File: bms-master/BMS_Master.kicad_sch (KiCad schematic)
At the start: 79 parts, among them J1 Conn_PWR, J2 PROG, J3 Conn_Fault, J4 BMS_M_IN, J5 Conn_CAN, J6 Conn_CSR, J7 Conn_CSROUT, J8 Micro_SD_Card, SW1 SW_SPST, U1 AP2204K-ADJ, U2 AP2204K-ADJ, U3 STM32F103C8Tx, U4 BQ79600-Q1, U5 SN65HVD256D, U6 TLV2371DBV, U7 TLV2371DBV, Y1 8M, Y2 32.768k

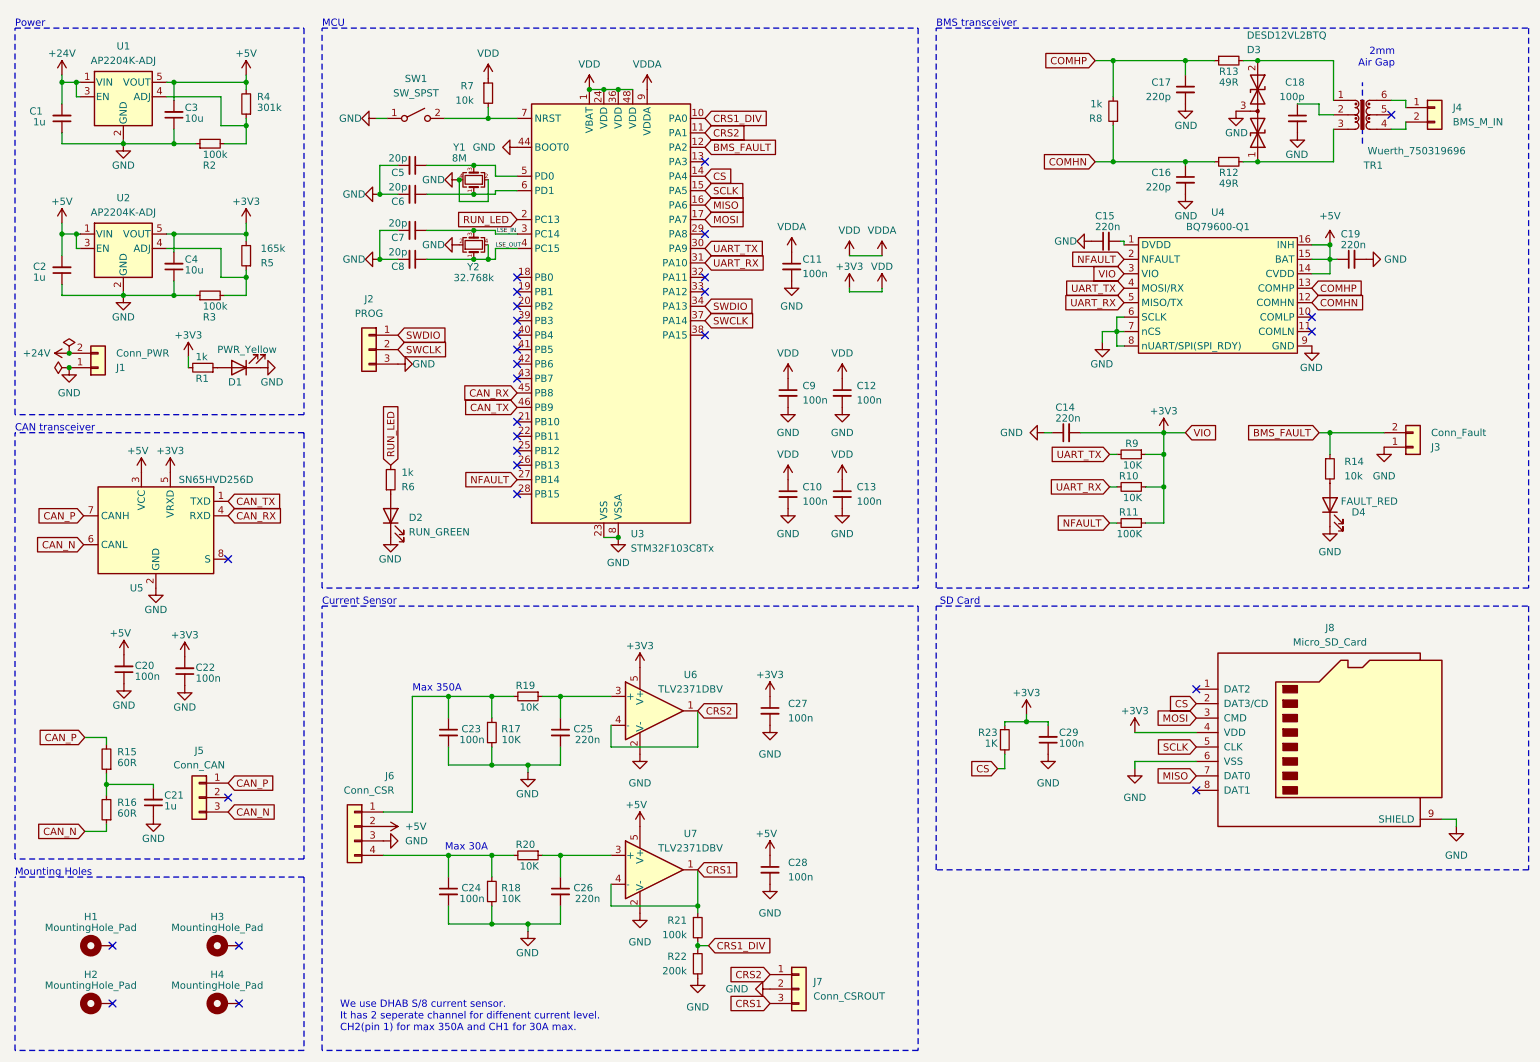
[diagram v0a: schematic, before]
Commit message: feat: wireless BMS and USB power
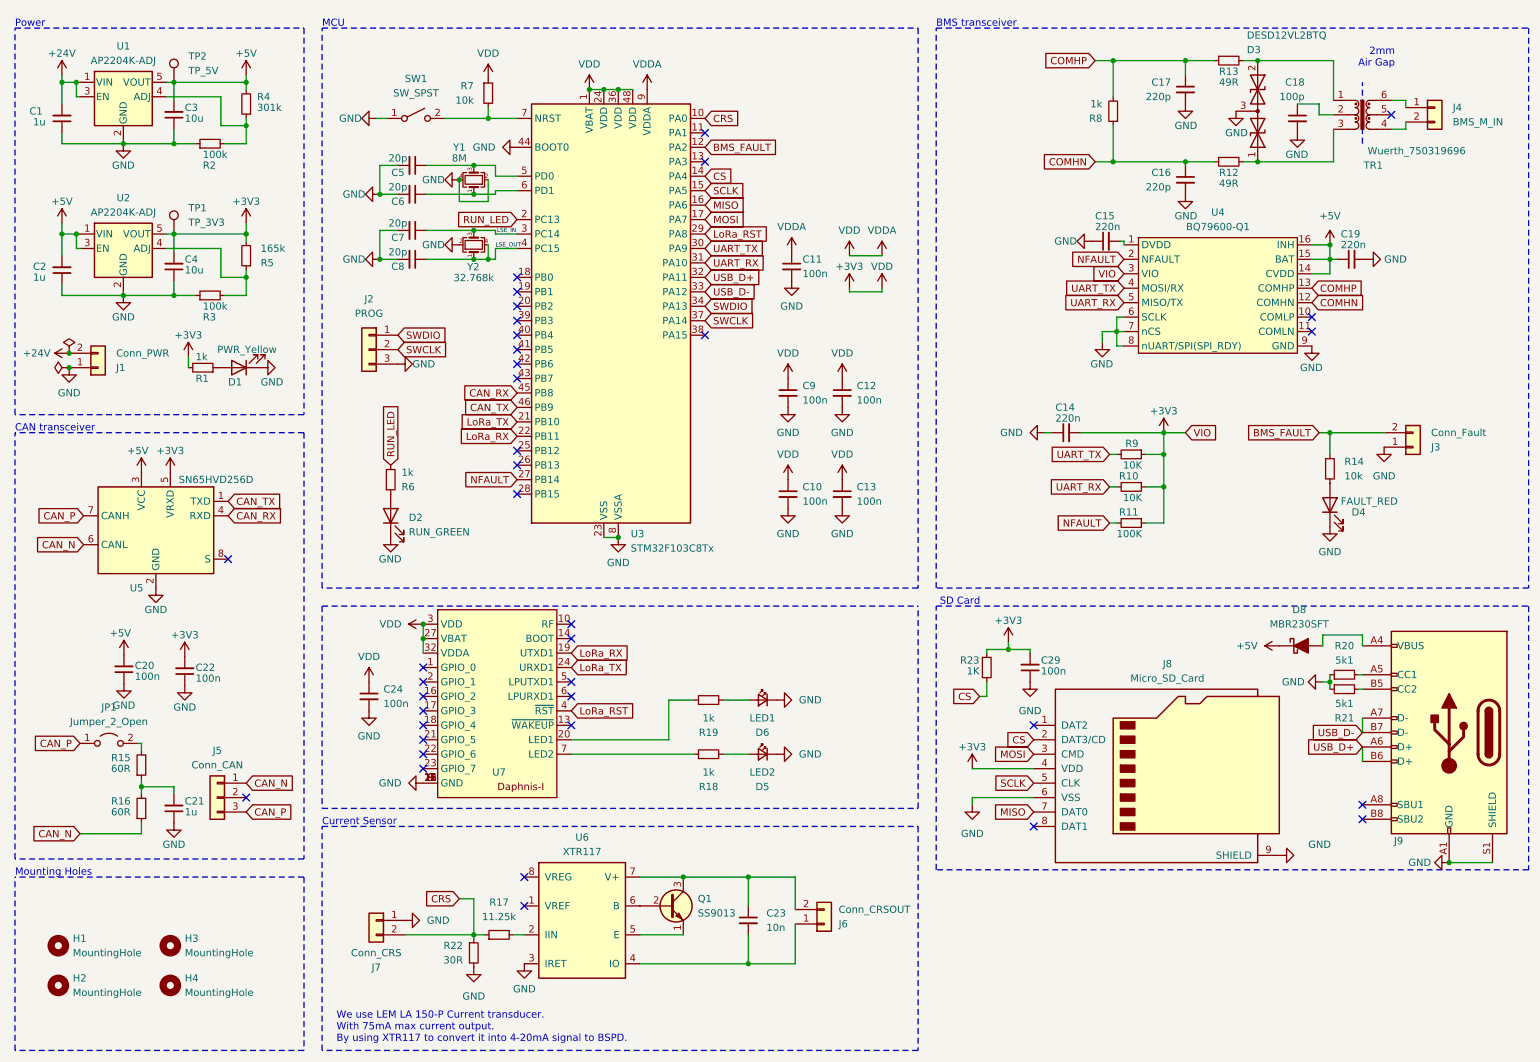
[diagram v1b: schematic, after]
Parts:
- removed C25, C26: 220n, Capacitor_SMD:C_0805_2012Metric, symbol Device:C_Small
- removed C27, C28: 100n, Capacitor_SMD:C_0603_1608Metric, symbol Device:C_Small
- removed H1, H2, H3, H4: MountingHole_Pad, MountingHole:MountingHole_3.2mm_M3_ISO14580_Pad, symbol Mechanical:MountingHole_Pad
- removed J6: Conn_CSR, Connector_JST:JST_XH_B4B-XH-A_1x04_P2.50mm_Vertical, symbol Connector_Generic:Conn_01x04
- removed J7: Conn_CSROUT, Connector_JST:JST_XH_B3B-XH-A_1x03_P2.50mm_Vertical, symbol Connector_Generic:Conn_01x03
- removed U6, U7: TLV2371DBV, Package_TO_SOT_SMD:SOT-23-5, symbol Amplifier_Operational:TLV2371DBV
- added D5: LED2, LED_SMD:LED_0805_2012Metric, symbol Device:LED_Small
- added D6: LED1, LED_SMD:LED_0805_2012Metric, symbol Device:LED_Small
- added D8: MBR230SFT, Diode_SMD:D_SOD-123F, symbol PCM_Diode_Schottky_AKL:MBR230SFT
- added H1, H2, H3, H4: MountingHole, MountingHole:MountingHole_3.2mm_M3_DIN965, symbol Mechanical:MountingHole
- added J6: Conn_CRSOUT, Connector_JST:JST_XH_B2B-XH-A_1x02_P2.50mm_Vertical, symbol Connector_Generic:Conn_01x02
- added J7: Conn_CRS, Connector_JST:JST_XH_B2B-XH-A_1x02_P2.50mm_Vertical, symbol Connector_Generic:Conn_01x02
- added J9: USB_C_Receptacle_USB2.0_16P, Connector_USB:USB_C_Receptacle_Palconn_UTC16-G, symbol Connector:USB_C_Receptacle_USB2.0_16P
- added JP1: Jumper_2_Open, PCM_Jumper_AKL:Jumper_P2.54mm_D0.7mm, symbol Jumper:Jumper_2_Open
- added Q1: SS9013, Package_TO_SOT_SMD:SOT-23, symbol PCM_Transistor_BJT_AKL:SS9013
- added TP1: TP_3V3, Connector_Pin:Pin_D1.0mm_L10.0mm, symbol Connector:TestPoint
- added TP2: TP_5V, Connector_Pin:Pin_D1.0mm_L10.0mm, symbol Connector:TestPoint
- added U6: XTR117, Package_SO:SOIC-8_3.9x4.9mm_P1.27mm, symbol Interface_CurrentLoop:XTR116U
- added U7: ~, Daphnis-I:Daphnis-I, symbol Project_Lib:Daphnis-I
- C23: value 100n -> 10n
- R17: value 10K -> 11.25k
- R18, R19: value 10K -> 1k
- R20: value 10K -> 5k1; footprint Resistor_SMD:R_0603_1608Metric -> Resistor_SMD:R_0603_1608Metric_Pad0.98x0.95mm_HandSolder
- R21: value 100k -> 5k1; footprint Resistor_SMD:R_0603_1608Metric -> Resistor_SMD:R_0603_1608Metric_Pad0.98x0.95mm_HandSolder
- R22: value 200k -> 30R
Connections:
- net CRS1 is gone; now on net GND: R21.1
- net +3V3: now also C24.1, TP1.1, U7.27 (VBAT), U7.3 (VDD), U7.32 (VDDA)
- net +5V: now also D8.1 (K), TP2.1
- net CAN_N: now also J5.1 (Pin_1); no longer J5.3 (Pin_3)
- net CAN_P: now also J5.3 (Pin_3), JP1.1 (A); no longer J5.1 (Pin_1), R15.2
- net GND: now also R20.1, D5.1 (K), D6.1 (K), J7.1 (Pin_1), J9.A1 (GND), J9.A12 (GND), J9.B1 (GND), J9.B12 (GND), J9.S1 (SHIELD), U6.3 (IRET), U7.11 (GND), U7.12 (GND), U7.15 (GND), U7.26 (GND), U7.8 (GND), U7.9 (GND); no longer C23.2, R17.2, R18.2
- net at R19.1: now also U7.20 (LED1)
- net LoRa_TX: now reaches U3.21 (PB10)
- net LoRa_TX: now also U7.24 (URXD1)
- net LoRa_RX: now reaches U3.22 (PB11)
- net LoRa_RX: now also U7.19 (UTXD1)
- net LoRa_RST: now reaches U3.29 (PA8)
- net LoRa_RST: now also U7.4 (~{RST})
- net USB_D+: now reaches U3.32 (PA11)
- net USB_D+: now also J9.A6 (D+), J9.B6 (D+)
- net USB_D-: now reaches U3.33 (PA12)
- net USB_D-: now also J9.A7 (D-), J9.B7 (D-)
- net CRS1_DIV renamed CRS
- net CRS: now also R17.1, J7.2 (Pin_2); no longer R21.2
- net CRS2: no longer names the net of U3.11 (PA1)
- new net: D8.2 (A), J9.A4 (VBUS), J9.A9 (VBUS), J9.B4 (VBUS), J9.B9 (VBUS)
- new net: J9.A5 (CC1), R20.2
- new net: J9.B5 (CC2), R21.2
- new net: JP1.2 (B), R15.2
- new net: R18.1, U7.7 (LED2)
- new net: R17.2, U6.2 (IIN)
- new net: C23.1, J6.2 (Pin_2), Q1.3 (C), U6.7 (V+)
- new net: C23.2, J6.1 (Pin_1), U6.4 (IO)
- new net: D5.2 (A), R18.2
- new net: D6.2 (A), R19.2
- new net: Q1.1 (E), U6.5 (E)
- new net: Q1.2 (B), U6.6 (B)
- no-connect marks 29 -> 38
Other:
- note added: "We use LEM LA 150-P Current transducer. With 75mA max current output. By using XTR117 to convert it into 4-20mA signal to BSPD."
- note removed: "Max 30A"
- note removed: "Max 350A"
- note removed: "We use DHAB S/8 current sensor. It has 2 seperate channel for diffenent current level. CH2(pin 1) for max 350A and CH1 for 30A max."
- moved on the sheet: C21, C29, J5, J8, R15, R16, R22, R23

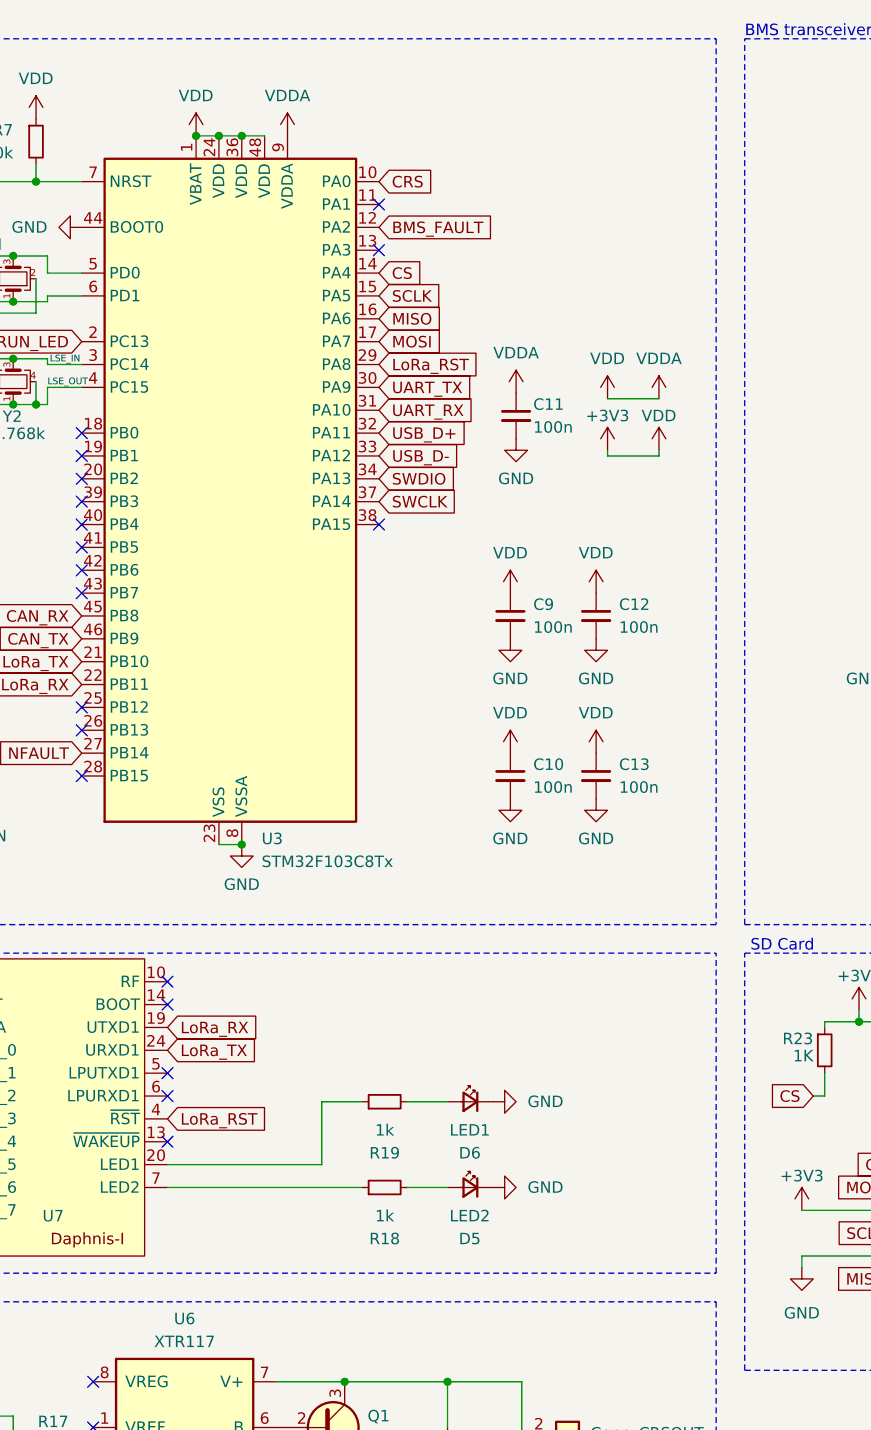
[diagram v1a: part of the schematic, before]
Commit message: fix: USB and USART traces
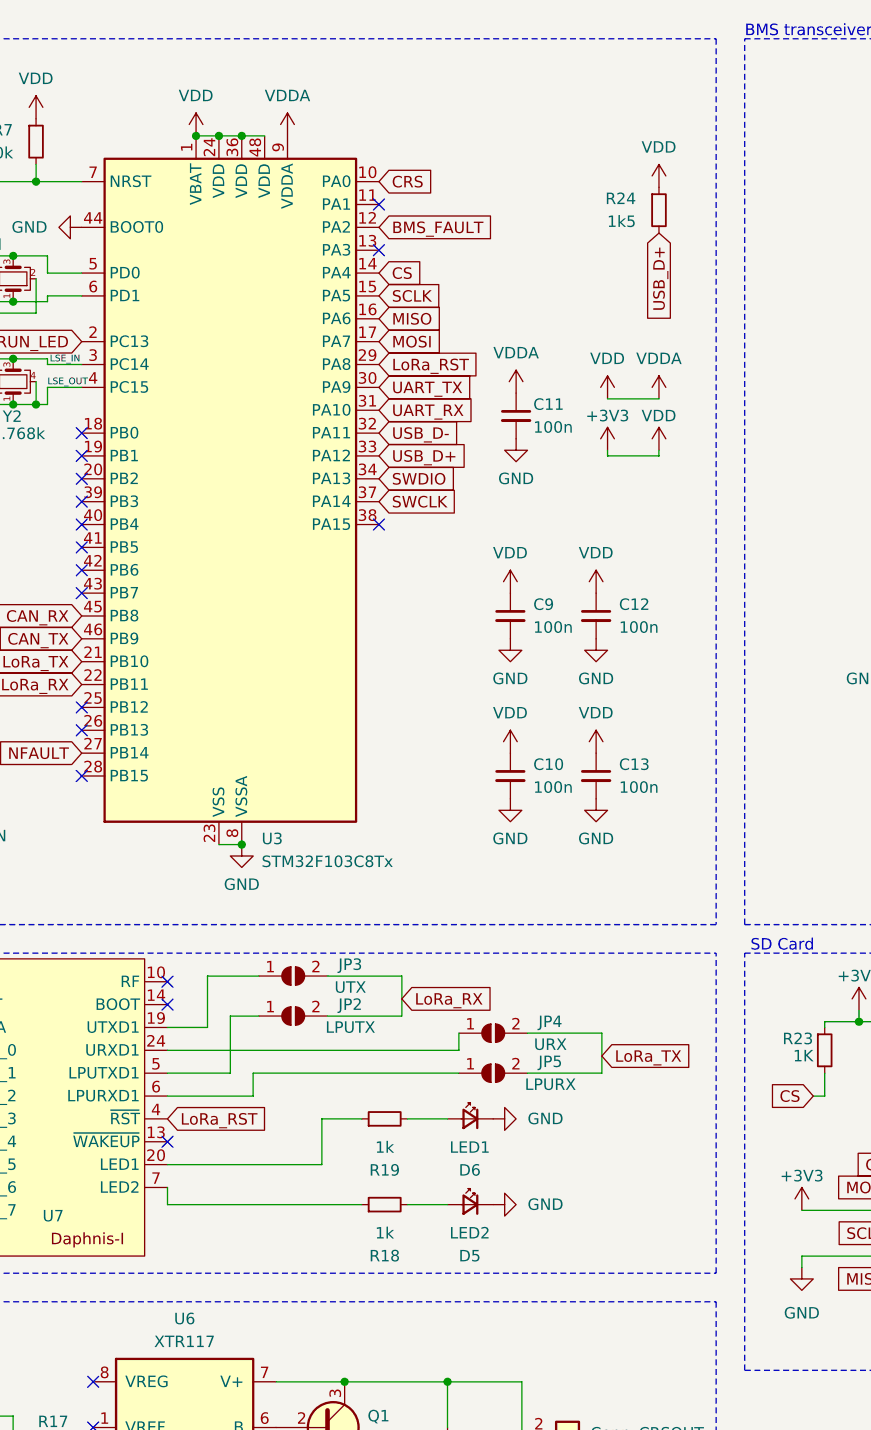
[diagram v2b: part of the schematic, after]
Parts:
- added JP2: LPUTX, Jumper:SolderJumper-2_P1.3mm_Open_RoundedPad1.0x1.5mm, symbol Jumper:SolderJumper_2_Open
- added JP3: UTX, Jumper:SolderJumper-2_P1.3mm_Open_RoundedPad1.0x1.5mm, symbol Jumper:SolderJumper_2_Open
- added JP4: URX, Jumper:SolderJumper-2_P1.3mm_Open_RoundedPad1.0x1.5mm, symbol Jumper:SolderJumper_2_Open
- added JP5: LPURX, Jumper:SolderJumper-2_P1.3mm_Open_RoundedPad1.0x1.5mm, symbol Jumper:SolderJumper_2_Open
- added R24: 1k5, Resistor_SMD:R_0603_1608Metric, symbol Device:R_Small
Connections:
- net +3V3: now also R24.1
- net LoRa_RX: now also JP2.2 (B), JP3.2 (B); no longer U7.19 (UTXD1)
- net LoRa_TX: now also JP4.2 (B), JP5.2 (B); no longer U7.24 (URXD1)
- net USB_D+: now also U3.33 (PA12), R24.2; no longer U3.32 (PA11)
- net USB_D-: now also U3.32 (PA11); no longer U3.33 (PA12)
- net at U7.5 (LPUTXD1): now also JP2.1 (A)
- net at U7.6 (LPURXD1): now also JP5.1 (A)
- new net: JP3.1 (A), U7.19 (UTXD1)
- new net: JP4.1 (A), U7.24 (URXD1)
- no-connect marks 38 -> 36
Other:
- moved on the sheet: D5, D6, R18, R19
